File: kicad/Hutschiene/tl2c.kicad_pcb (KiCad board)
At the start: 4 copper layers, 175.9 x 86.5 mm, 86 parts, among them IC101 ATTINY20-X, P101 12VDC, P102 RJ45, P103 CTL CONN, P104 TPI Header, P105 DRV CONN, P106 240VAC, P108 UG, P109 5VDC, P110 EG, P111 OG, P201 Mode_Bridge, P501 CONN_PIR_OG, P502 CONN_PIR_EG, P503 CONN_PIR_UG, Q301 IRLML2502, Q302 IRLML2502, Q303 IRLML2502, Q401 IRLML2502, Q402 IRLML2502, Q403 IRLML2502, SW101 TL3315NF160Q, U201 LF120ABDT-TR, U202 TPS70933

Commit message: Pushed the boards to OSHPark
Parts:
- moved G*** 7.48 mm to (164.0, 121.4), turned to 0 degrees
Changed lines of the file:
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@@
     (tags "capacitor 0805")
     (attr smd)
-    (fp_text reference C201 (at -1.016 -1.524 180) (layer B.SilkS)
+    (fp_text reference C201 (at 0 1.57 180) (layer B.SilkS)
       (effects (font (size 0.762 0.762) (thickness 0.127)) (justify mirror))
     )
@@
     (tags "resistor 0805")
     (attr smd)
-    (fp_text reference R202 (at -0.0127 -1.4859) (layer B.SilkS)
+    (fp_text reference R202 (at -3.22 0.57) (layer B.SilkS)
       (effects (font (size 0.762 0.762) (thickness 0.127)) (justify mirror))
     )
@@
   )
   (module tl2c-footprint:MyBasic_rounded_50_1 locked (layer F.Cu)
-    (at 157.98 116.99 90)
-    (fp_text reference G*** (at 0 0 90) (layer F.SilkS) hide
+    (at 164.04 121.37)
+    (fp_text reference G*** (at 0 0) (layer F.SilkS) hide
       (effects (font (thickness 0.3)))
     )
-    (fp_text value LOGO (at 0.75 0 90) (layer F.SilkS) hide
+    (fp_text value LOGO (at 0.75 0) (layer F.SilkS) hide
       (effects (font (thickness 0.3)))
     )
@@
     (effects (font (size 0.762 0.762) (thickness 0.127)) (justify left))
   )
-  (gr_text GND (at 102.64 73.04 180) (layer F.SilkS)
+  (gr_text GND (at 102.45 71.51 180) (layer F.SilkS)
     (effects (font (size 1.27 1.27) (thickness 0.1778)))
   )
-  (gr_text +12V (at 107.71 73.15 180) (layer F.SilkS)
+  (gr_text +12V (at 107.94 71.44 180) (layer F.SilkS)
     (effects (font (size 1.27 1.27) (thickness 0.1778)))
   )
@@
     (effects (font (size 1.27 1.27) (thickness 0.1778)))
   )
-  (gr_text "L\nIN" (at 97.25 133.25) (layer F.SilkS)
+  (gr_text "L\nIN" (at 102.71 133.83) (layer F.SilkS)
     (effects (font (size 1.27 1.27) (thickness 0.1778)))
   )
@@
     (effects (font (size 1.27 1.27) (thickness 0.1778)))
   )
-  (gr_text N (at 102.3 133.95) (layer F.SilkS)
+  (gr_text N (at 107.46 134.36) (layer F.SilkS)
     (effects (font (size 1.778 1.778) (thickness 0.254)))
   )
@@
     (effects (font (size 1.27 1.27) (thickness 0.127)) (justify mirror))
   )
-  (gr_text 5V (at 215.47 120.52 90) (layer F.SilkS)
-    (effects (font (size 0.762 0.762) (thickness 0.127)))
+  (gr_text 5V (at 215.22 120.48 90) (layer B.SilkS)
+    (effects (font (size 0.762 0.762) (thickness 0.127)) (justify mirror))
   )
   (gr_text * (at 186.82 108.47 90) (layer B.SilkS)
@@
   )
   (gr_line (start 70.259 133.0008) (end 70.259 135.1852) (angle 90) (layer F.SilkS) (width 0.2))
-  (gr_line (start 100.1138 133.0008) (end 100.1138 135.1852) (angle 90) (layer F.SilkS) (width 0.2))
+  (gr_line (start 105.0638 133.1708) (end 105.0638 135.3552) (angle 90) (layer F.SilkS) (width 0.2))
   (gr_text "L\nEG" (at 67.15 133.55) (layer F.SilkS)
     (effects (font (size 1.27 1.27) (thickness 0.1778)))
@@
     (effects (font (size 0.762 0.762) (thickness 0.127)))
   )
-  (gr_text "Timed LED Lighting \nController 4L_2_CTRL\nControl Board" (at 162.78 120.1 90) (layer F.SilkS)
+  (gr_text "Timed LED Lighting \nController 4L_2_CTRL\nControl Board" (at 167.95 121.32) (layer F.SilkS)
     (effects (font (size 0.762 0.762) (thickness 0.127)) (justify left))
   )

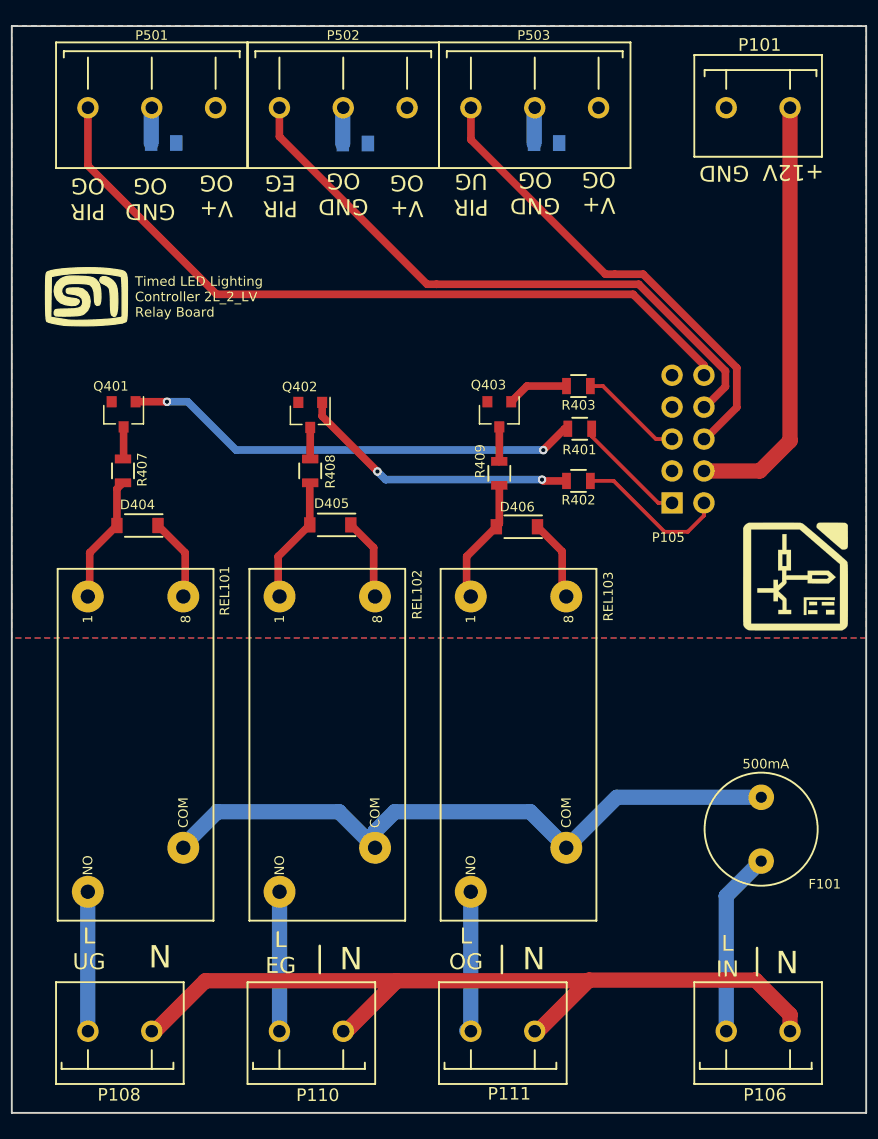
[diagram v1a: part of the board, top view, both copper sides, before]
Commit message: Corrections to the terminal block drill holes
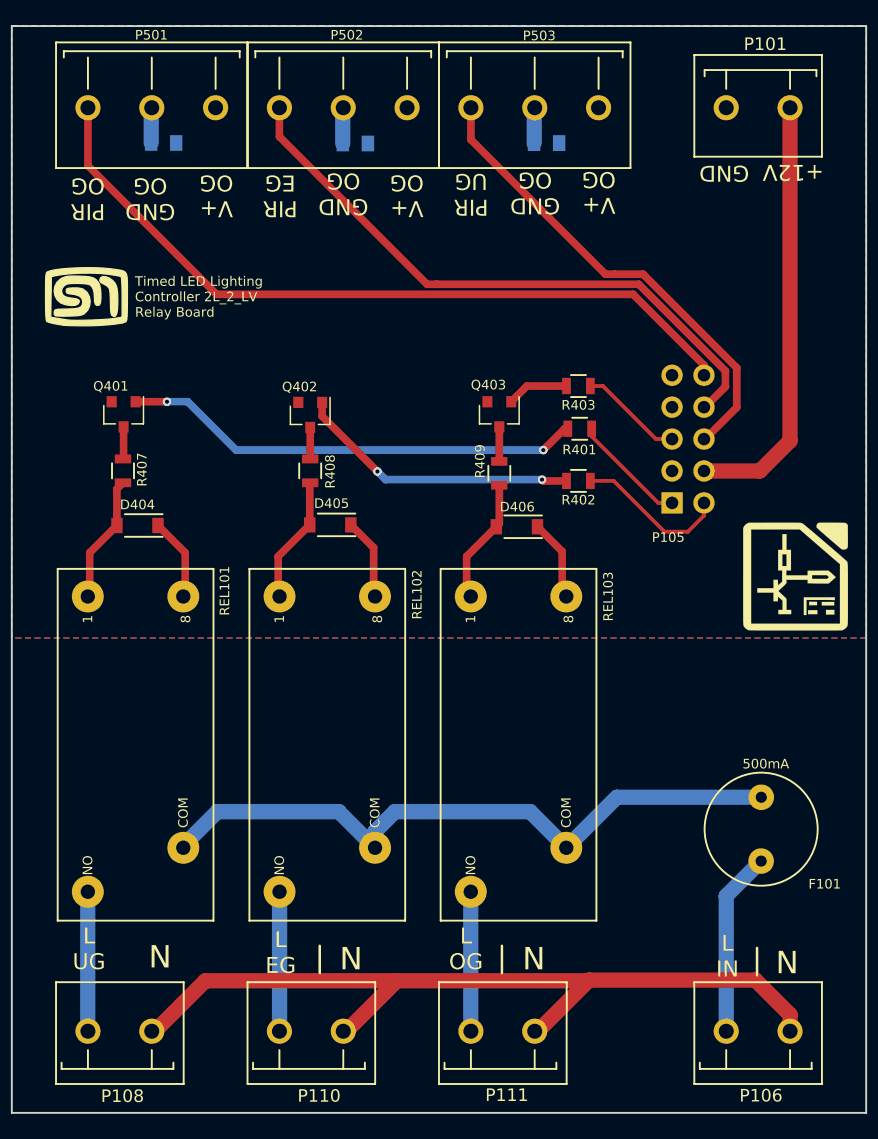
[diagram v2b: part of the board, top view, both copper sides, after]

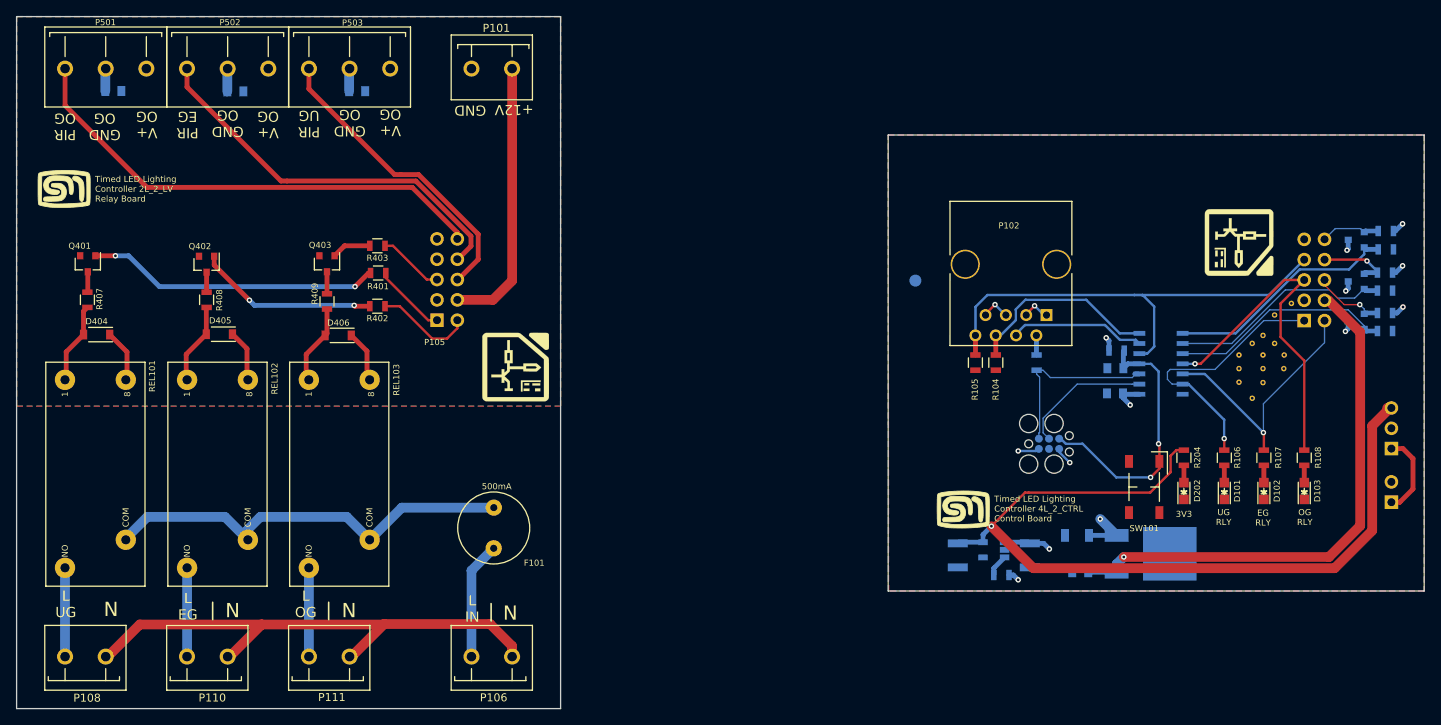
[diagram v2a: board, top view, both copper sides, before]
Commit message: Flipped the RJ45 to the bottom
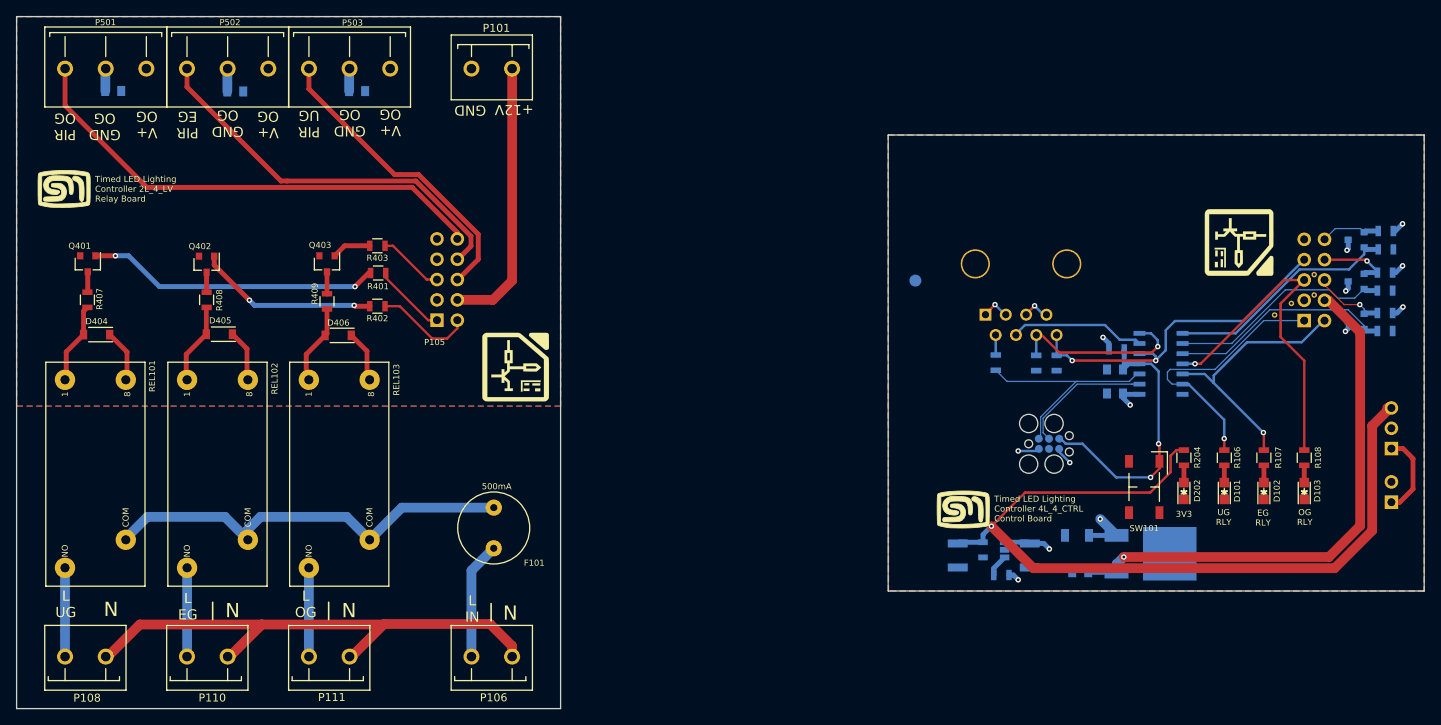
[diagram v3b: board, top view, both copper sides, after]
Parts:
- removed REF** (x2), REF**11, REF**12, REF**13, REF**21, REF**22, REF**32, REF**41, REF**42: Stitch_VIA, tl2c-footprint:Stitch_VIA
- removed the REF**31 at (203.0, 100.7)
- removed the REF**31 at (201.6, 102.1)
- added REF**31: Stitch_VIA, tl2c-footprint:Stitch_VIA, F.Cu at (207.9, 92.0)
- added REF**31: Stitch_VIA, tl2c-footprint:Stitch_VIA, F.Cu at (207.9, 94.6)
- P102, R104, R105: moved to B.Cu
- moved P102 10.2 mm to (175.8, 99.6), turned to 0 degrees
- moved R105 10.2 mm to (175.8, 103.1)
- moved R103 5.10 mm to (168.2, 103.0)
- moved R104 5.05 mm to (173.2, 103.1)
- moved C102 0.16 mm to (183.1, 103.9)
- moved R101 0.15 mm to (183.2, 101.4)
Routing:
- net /GPIO_PB2: track 60.4 -> 43.6 mm, vias 0 -> 2
- net /TPIDATA: track 22.8 -> 28.5 mm
- net /RLY_INT: track 24.8 -> 22.4 mm, vias 0 -> 1
- net /SDA: track 2.47 -> 3.12 mm
- net /~Reset: track 34.9 -> 35.5 mm
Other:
- board text added: "Timed LED Lighting Controller 2L_4_LV Relay Board"
- board text added: "Timed LED Lighting Controller 4L_4_CTRL Control Board"
- board text removed: "Timed LED Lighting Controller 2L_2_LV Relay Board"
- board text removed: "Timed LED Lighting Controller 4L_2_CTRL Control Board"

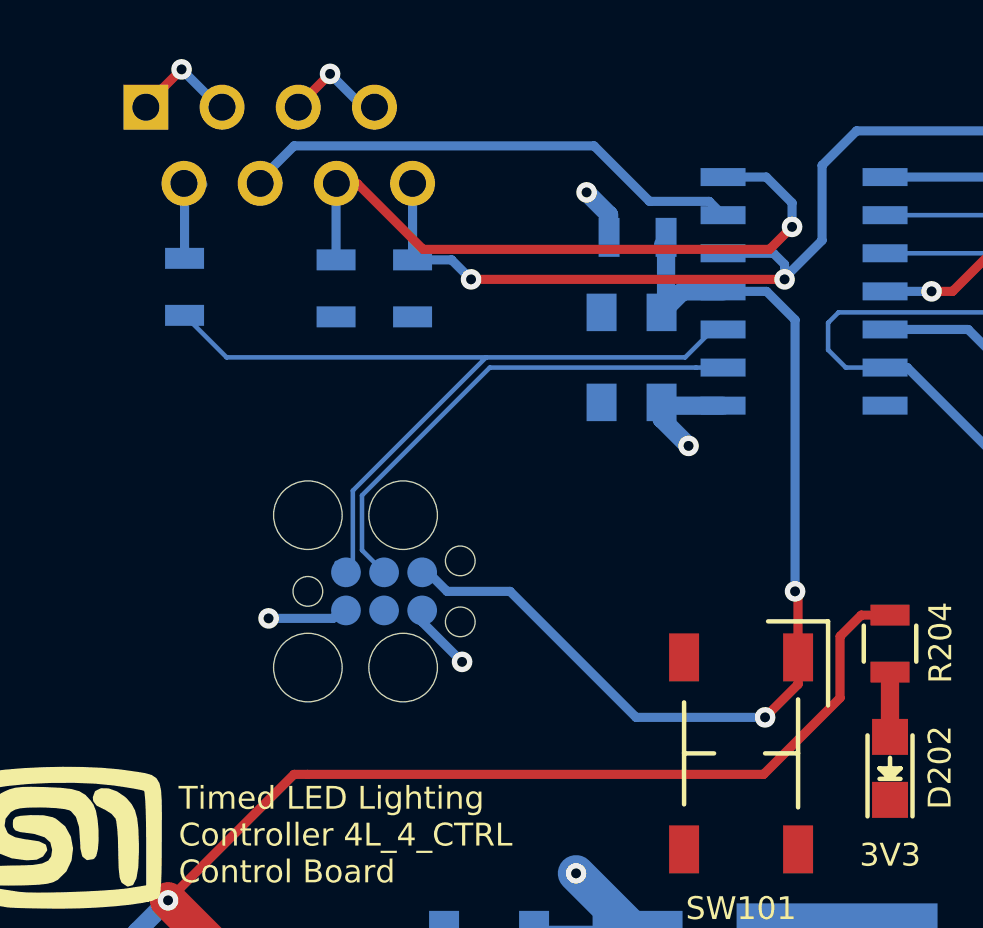
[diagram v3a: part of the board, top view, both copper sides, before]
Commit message: Flipped the programming head to the bottom
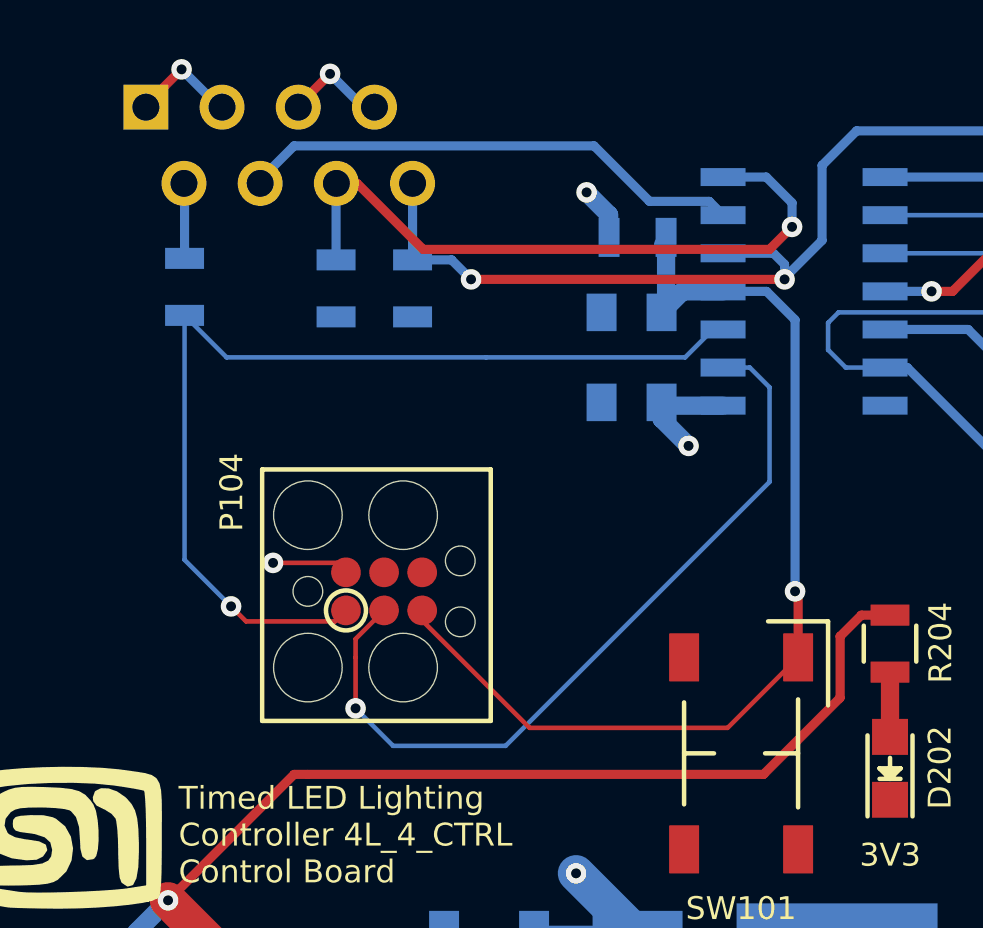
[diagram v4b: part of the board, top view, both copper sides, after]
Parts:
- P104: moved to F.Cu
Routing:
- net /TPICLK: track 16.7 -> 26.6 mm, vias 0 -> 1
- net /TPIDATA: track 28.5 -> 33.4 mm, vias 0 -> 1
- net GND: track 9.52 -> 7.25 mm, vias 3 -> 2
- net /SDA: track 3.12 -> 2.51 mm
- net /~Reset: track 35.5 -> 34.9 mm, vias 2 -> 1

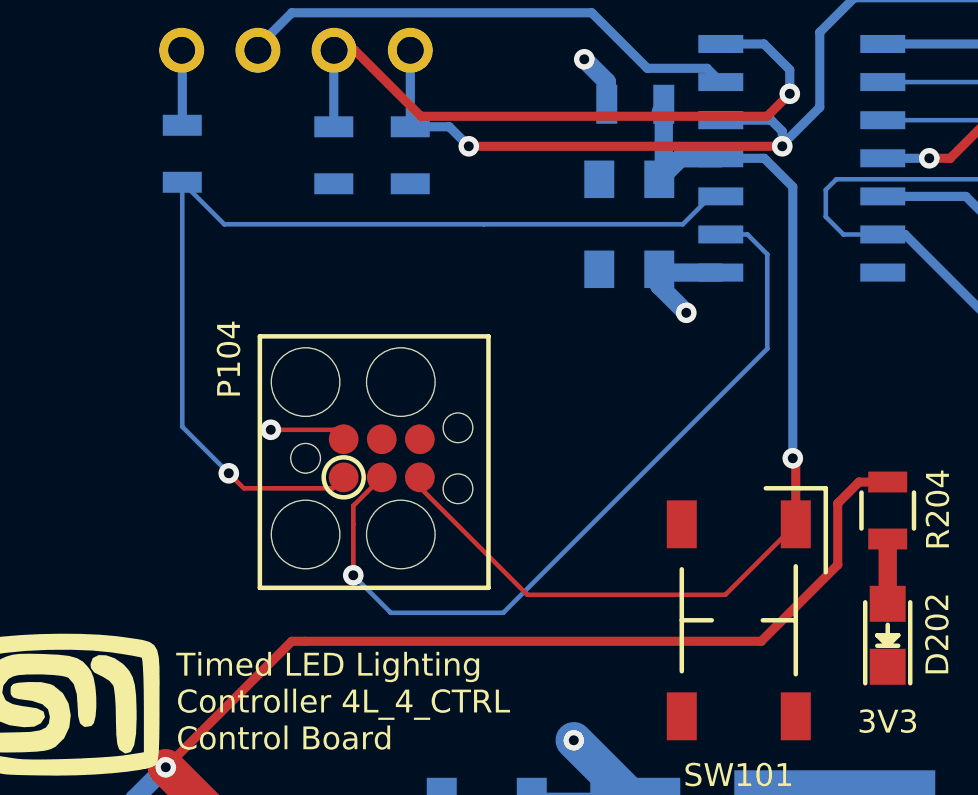
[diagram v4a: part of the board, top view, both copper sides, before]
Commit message: Flipped the programming header to the bottom (correct layout)
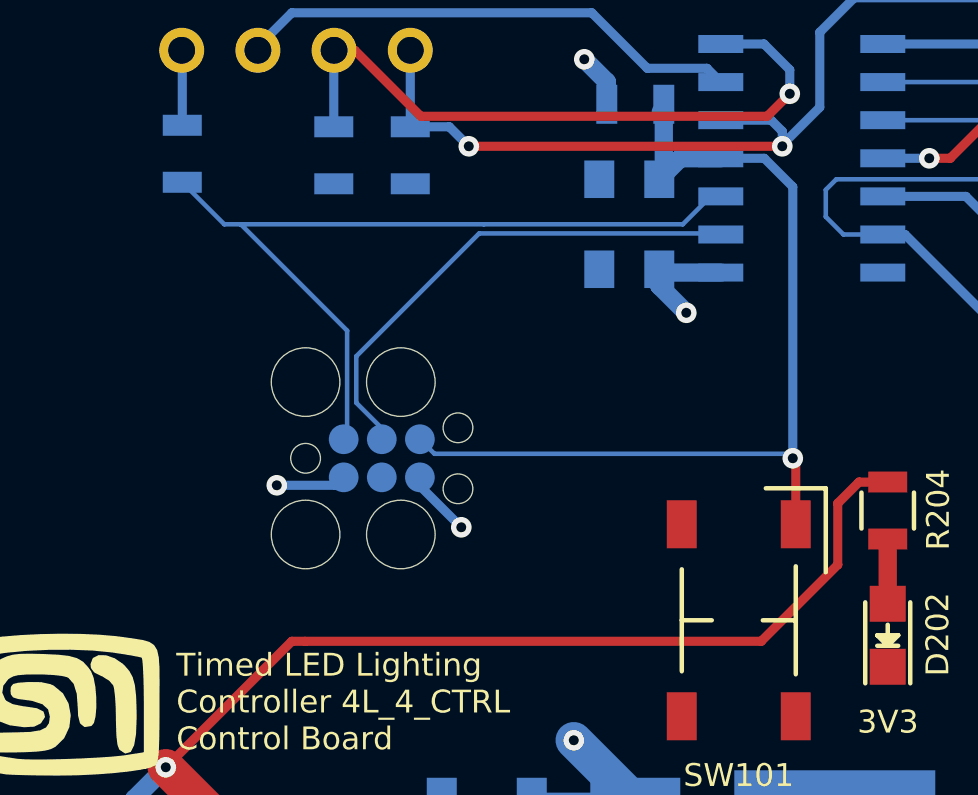
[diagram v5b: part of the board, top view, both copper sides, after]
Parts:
- P104: moved to B.Cu
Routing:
- net /TPICLK: track 26.6 -> 17.0 mm, vias 1 -> 0
- net /TPIDATA: track 33.4 -> 27.6 mm, vias 1 -> 0
- net /~Reset: track 34.9 -> 32.3 mm
- net GND: track 7.25 -> 9.49 mm, vias 2 -> 3
